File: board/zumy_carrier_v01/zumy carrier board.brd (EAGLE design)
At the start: 54 x 88.9 mm, 17 parts, among them M1 POLOLU_STEP_DOWN, M2 ITG/MPU_MODULE, M3 POLOLU_DRV8833_MODULE, SW1 500SSP1S1M6QEA

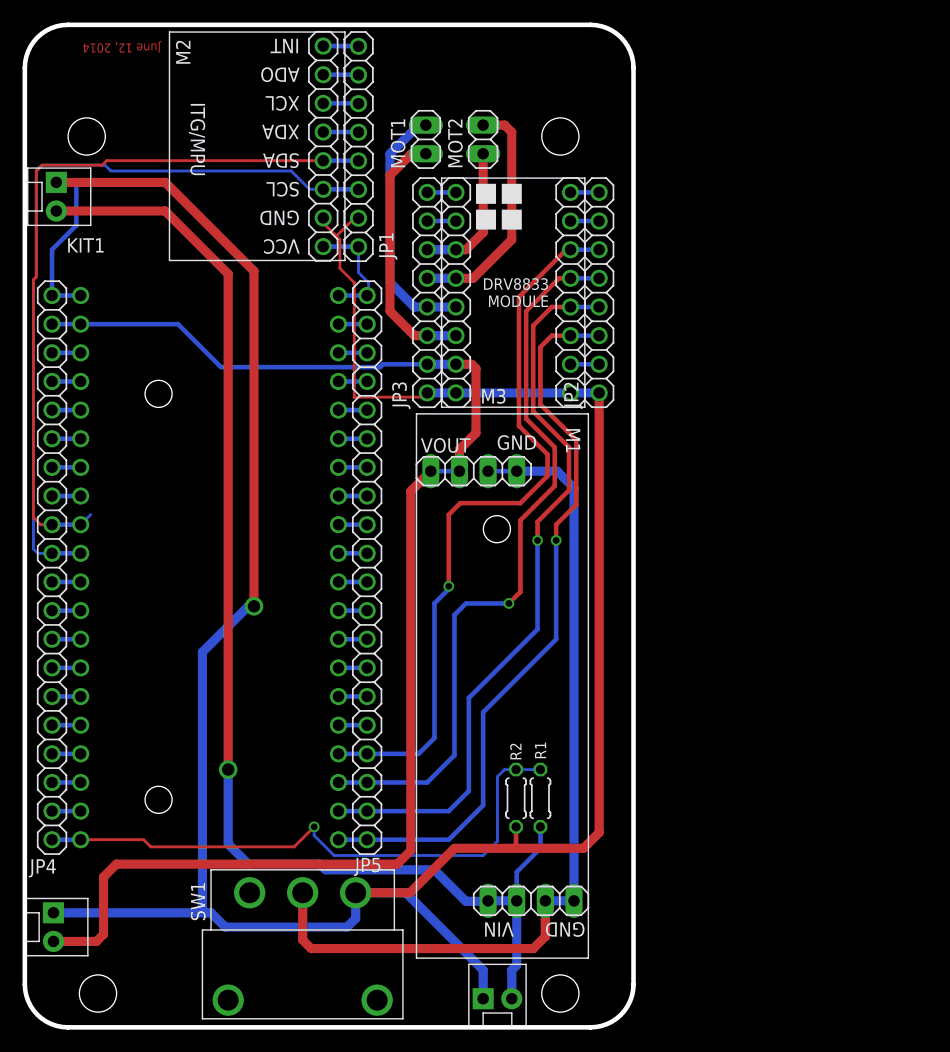
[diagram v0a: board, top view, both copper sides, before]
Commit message: Preliminary updates for rev c, unrouted.
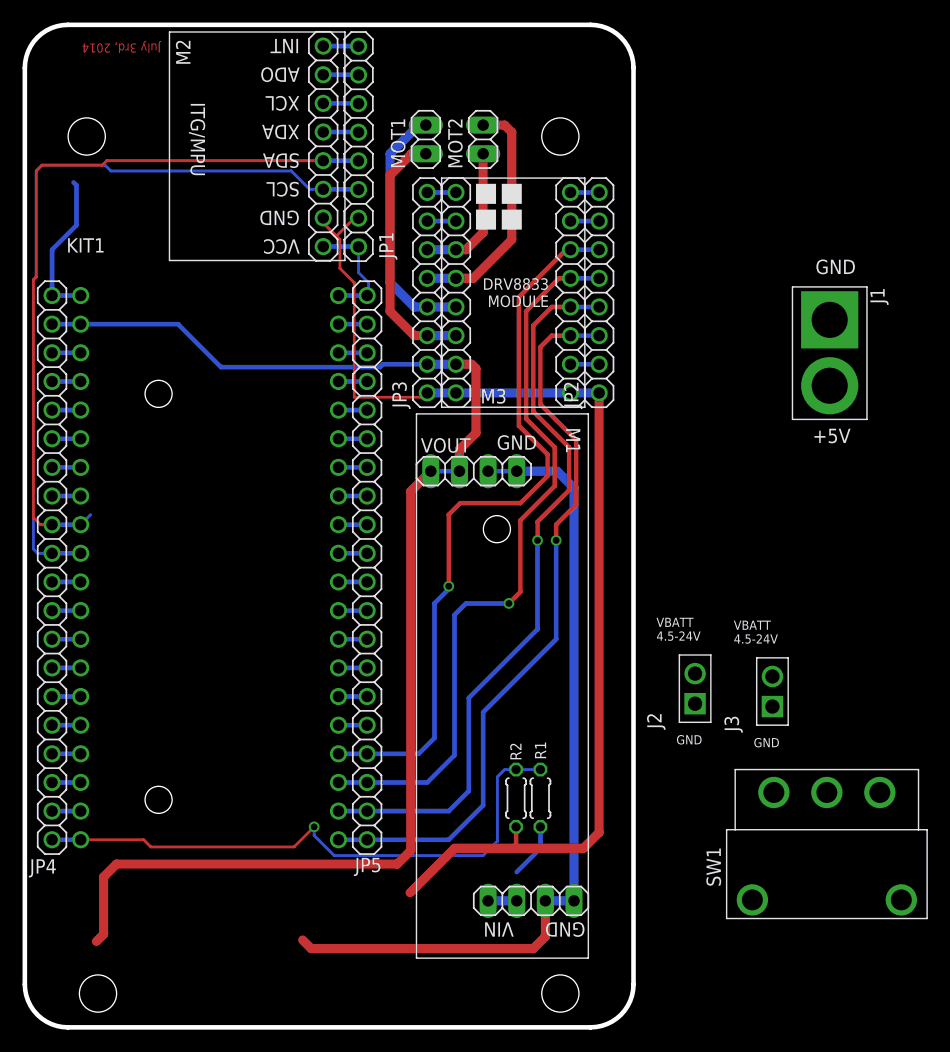
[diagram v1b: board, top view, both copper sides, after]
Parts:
- removed JP6, JP7, ODROID: M02POLAR, SparkFun-Connectors:MOLEX-1X2
- added J1: ODROID_POWER, zumy:ODOIRD_PWR
- added J2, J3: BATT_POWER, zumy:BATT_POWER
- moved SW1 47.3 mm to (71.1, 20.8)
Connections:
- new net N$5: J1.GND, JP1.7, M2.GND
- new net SW_VBATT: M1.VIN1, M1.VIN2, SW1.1
- net +5V: now also J1.PWR; no longer ODROID.2
- net GND: now also J2.GND, J3.GND; no longer JP1.7, JP6.1, JP7.1, M2.GND, ODROID.1, SW1.1
- net N$65: no longer SW1.2
- net VBATT: now also J2.PWR, J3.PWR, SW1.2; no longer JP6.2, JP7.2, M1.VIN1, M1.VIN2
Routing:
- net GND: track 248.4 -> 114.6 mm, vias 1 -> 0
- net VBATT: track 112.1 -> 4.88 mm, vias 1 -> 0
- net N$65: track 77.0 -> 72.8 mm
- net +5V: track 124.1 -> 120.2 mm
- net SW_VBATT: track 0.00 -> 2.54 mm
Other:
- board text added: "July 3rd, 2014"
- board text added: "Rev C"
- board text removed: "June 12, 2014"
- board text removed: "Rev B"

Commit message: added rev c zumy carrier board
expanded odroid power holes
expanded battery power holes
module layout change
fixed switching cicuit to switch battery rather than ground
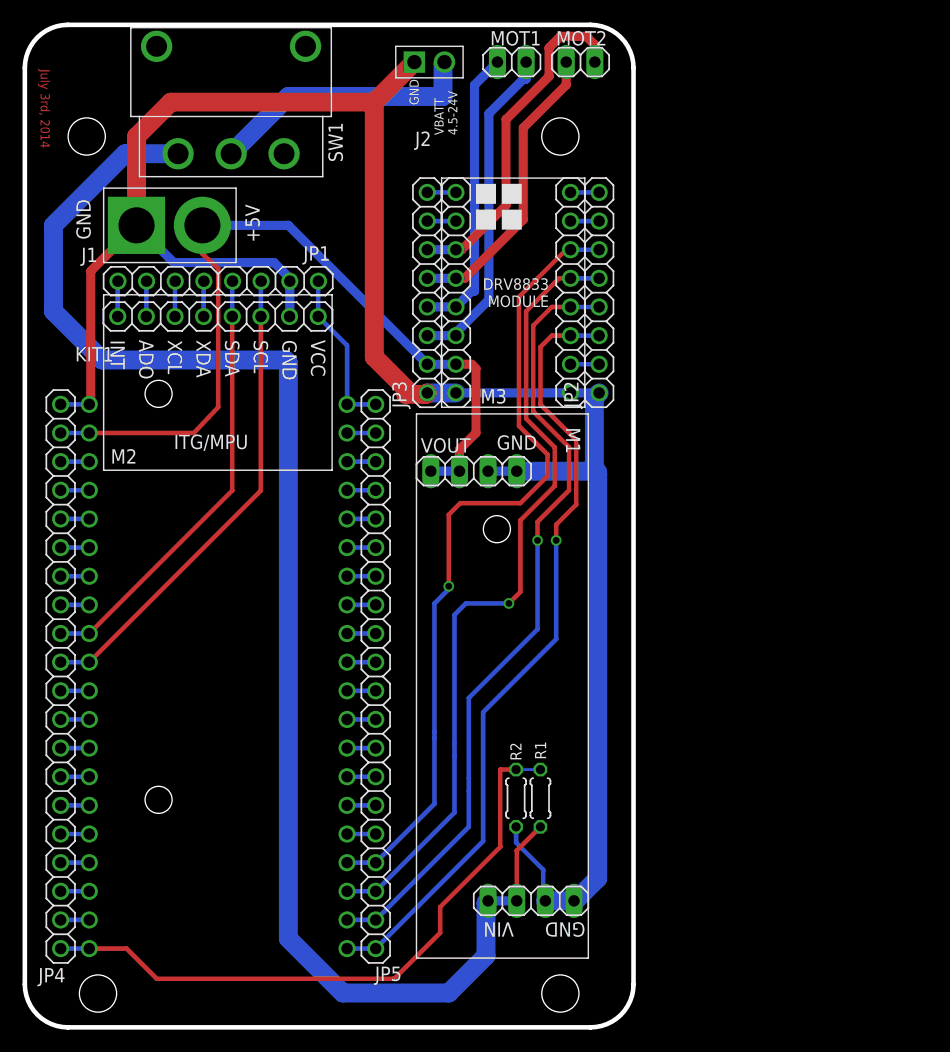
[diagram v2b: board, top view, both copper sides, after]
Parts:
- removed J3: BATT_POWER, zumy:BATT_POWER
- moved SW1 77.5 mm to (18.3, 77.5), turned to 0 degrees
- moved J2 62.1 mm to (34.5, 85.6), turned to 0 degrees
- moved J1 62.0 mm to (9.91, 71.1), turned to 0 degrees
- moved M2 22.4 mm to (17.1, 55.8), turned to 0 degrees
- moved JP1 17.2 mm to (17.1, 66.2), turned to 0 degrees
- moved MOT2 11.0 mm to (49.3, 85.6), turned to 180 degrees
- moved MOT1 10.3 mm to (43.2, 85.6), turned to 180 degrees
- moved JP4 9.68 mm to (3.17, 31.1)
- moved JP5 9.68 mm to (31.1, 31.1)
- moved KIT1 9.68 mm to (17.1, 31.1)
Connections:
- removed net N$5: J1.GND, JP1.7, M2.GND
- removed net N$65: M1.GND1, M1.GND2, M1.GND3, M1.GND4
- net GND: now also J1.GND, JP1.7, M1.GND1, M1.GND2, M1.GND3, M1.GND4, M2.GND; no longer J3.GND
- net SW_VBATT: now also R1.2
- net VBATT: no longer J3.PWR, R1.2
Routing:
- net SW_VBATT: track 2.54 -> 130.9 mm
- net N$65: track 72.8 -> 0.00 mm
- net GND: track 114.6 -> 185.3 mm
- net +5V: track 120.2 -> 73.5 mm
- net MPU_SDA: track 65.7 -> 39.2 mm
- net MPU_SCL: track 67.9 -> 42.8 mm
- net VBATT: track 4.88 -> 24.0 mm
- net N$62: track 12.6 -> 30.5 mm
- net N$59: track 22.8 -> 29.5 mm
- net AIN1: track 65.4 -> 72.0 mm
- net AIN2: track 65.3 -> 71.5 mm
- net BIN2: track 65.1 -> 70.2 mm
- net BIN1: track 65.1 -> 70.2 mm
- net N$61: track 21.2 -> 26.2 mm
- net V_BATT_SENSE: track 52.3 -> 56.7 mm, vias 1 -> 0
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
